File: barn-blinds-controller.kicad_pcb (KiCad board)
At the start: 4 copper layers, 65 x 73.9 mm, 112 parts, among them J1 DC005-T20, J2 USB_B_Micro, J3 Conn_01x07, J4 Phoenix Contact 1786918, Q1 2N7002, Q2 2N7002, Q3 S8050, Q4 S8050, SW1 RESET, SW2 BOOT, U1 DCDC Converter, U10 TMP235, U11 ACS723xLCTR-05AB, U12 PRTR5V0U2X, U13 PRTR5V0U2X, U14 PRTR5V0U2X, U15 PRTR5V0U2X, U2 AP2112K-3.3, U3 ESP32-S3-WROOM-1, U4 ISO7760DBQ, U5 ISO7760DBQ, U6 ISO7760DBQ, U7 AMS1117-3.3, U8 TB6612FNG, U9 TB6612FNG

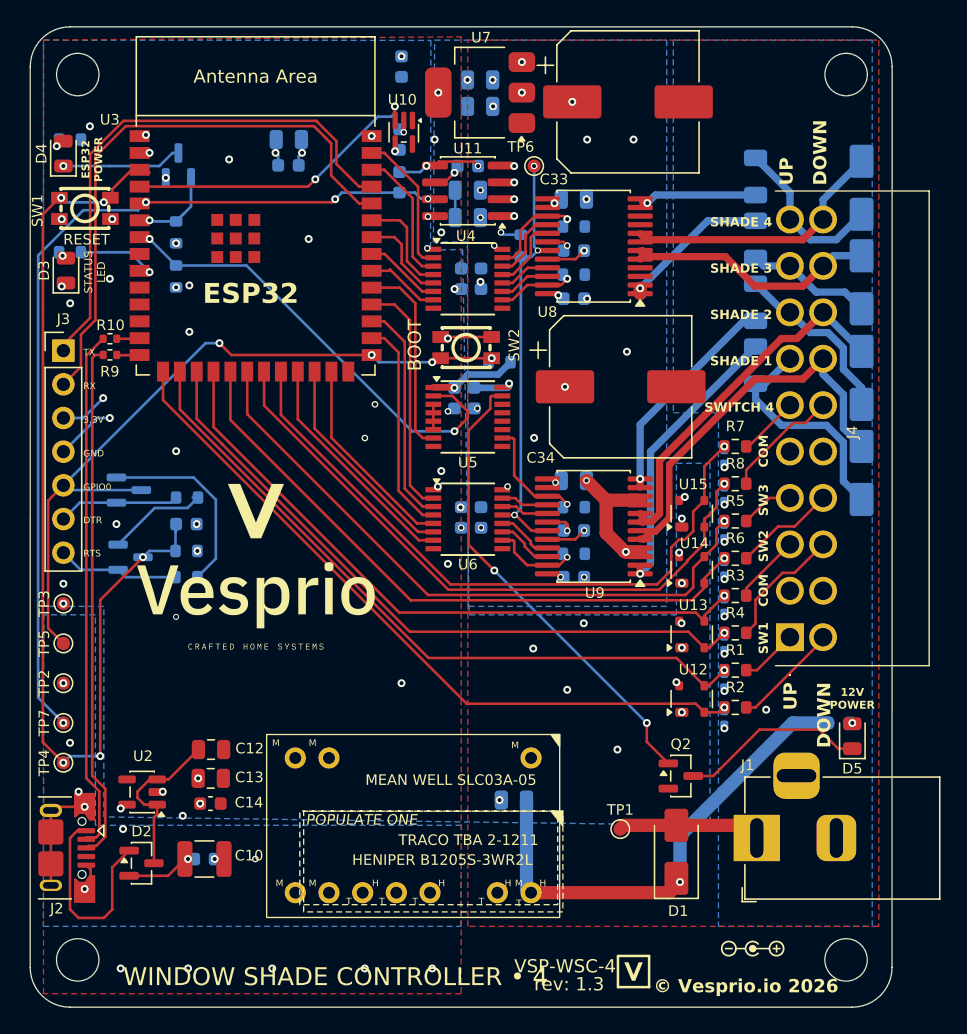
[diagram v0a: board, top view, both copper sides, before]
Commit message: Rev 1.3 PCB sync + second QA pass: BOM fixes, TVS decoupling, ERC cleanup
PCB (done in KiCad, verified here):
- F8 sync applied: D2 removed; D10/D11 (SS34 SMA) and U16 (PRTR5V0U2X SOT-143)
  placed and routed; R1-R8 -> 1k, D1 -> SS54, C10 -> 25V, U11 -> ACS725 updated
  in place. Footprint-level diff confirms exactly the intended delta, nothing
  else moved. DRC 0 errors / 0 unconnected pads.

Schematic fixes from the second QA pass:
- R1-R8 had NO LCSC part number (value change had landed, part number never
  did) - they would have come back unpopulated, silently killing the switch
  inputs. Set to C14676, matching R14's existing 1K 0603 so it consolidates to
  one BOM line. NOTE: todo.md originally specified C21190 - see the discrepancy
  note there and confirm before ordering.
- TP1-TP7 set in_bom no / in_pos_files no (were 7 junk lines in the JLCPCB BOM).
- Removed 4 orphan dangling wire stubs in switch_inputs.kicad_sch.
- Converted the orphan STBY hierarchical label in motor_drivers.kicad_sch to a
  global label rather than deleting it: its wire actually carried U9 pin 19, so
  deleting dropped U9.19 off the STBY net. Converting keeps the connection and
  clears the ERC hier_label_mismatch.
- Added C40-C43 (100nF 0402, C1525) for U12-U15 VCC decoupling. The switch-input
  TVS devices currently have their nearest +3.3V_ISO bypass 18-23mm away; a
  PRTR5V0U2X shunts ESD into VCC and needs somewhere local to dump it. Still
  need PCB placement - put each within ~2mm of its device's pin 4.

Every schematic edit was validated by diffing the exported netlist before and
after; connectivity is unchanged apart from the four intended new caps.
ERC errors: 10 -> 5 (remaining are 4x missing PWR_FLAG and one J2-GND/U1-(-Vout)
both-power-output pair that is correct by design).

Added barn-blinds-controller.kicad_dru: isolation-barrier audit rule. The board
has no dedicated ISO/MOTOR gap - minimum copper spacing between domains is
0.20mm, the global default. Rev 1.2 measured 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
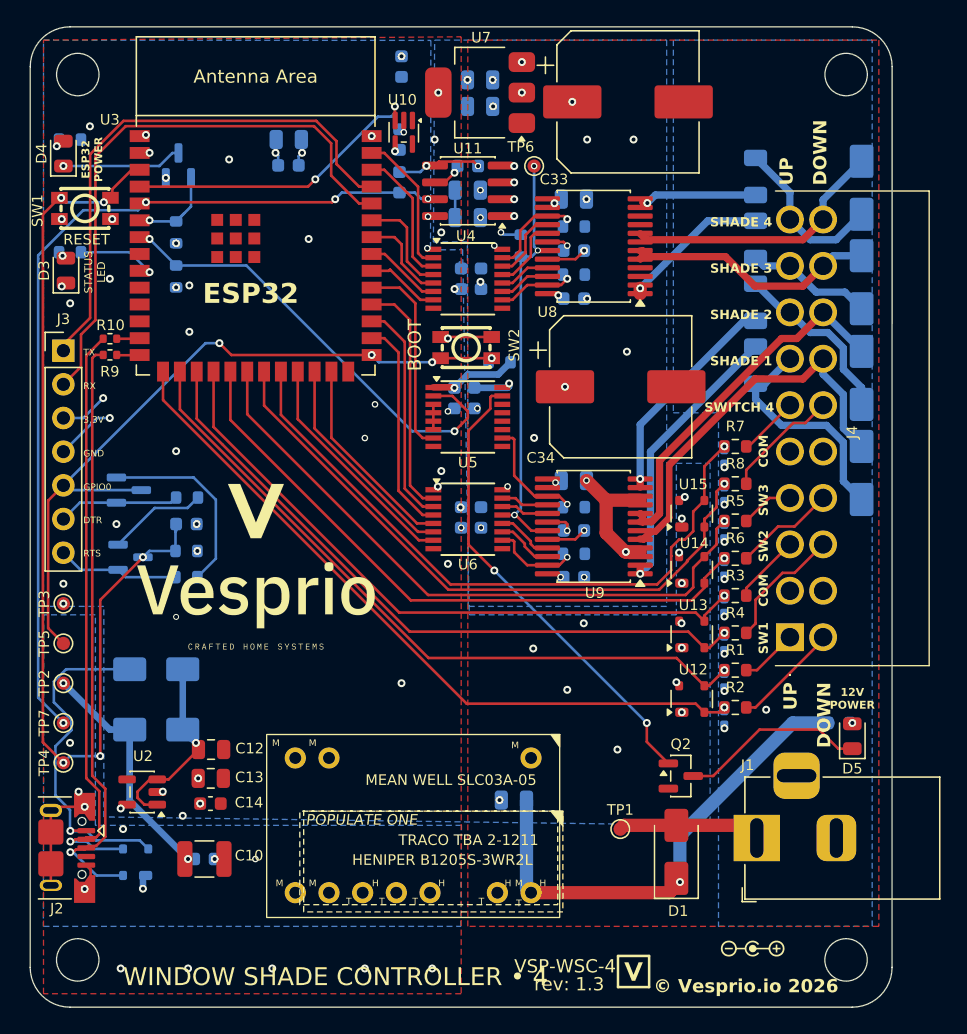
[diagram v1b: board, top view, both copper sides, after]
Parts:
- removed D2: BAT54C, Package_TO_SOT_SMD:SOT-23
- added D10: SS34, Diode_SMD:D_SMA, B.Cu at (86.5, 97.5)
- added D11: SS34, Diode_SMD:D_SMA, B.Cu at (86.5, 102.0)
- added U16: PRTR5V0U2X, Package_TO_SOT_SMD:SOT-143, B.Cu at (85.0, 112.0)
- C10: value 100uF 10V -> 100uF 25V
- D1: value SS34 -> SS54
- R1, R2, R3, R4, R5, R6, R7, R8: value 10k -> 1k
- U11: value ACS723xLCTR-05AB -> ACS725LLCTR-05AB-T
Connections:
- J2 pad 1: Net-(J2-VBUS) -> /USB-C and 5V Diode-OR/USB_VBUS
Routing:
- net /USB-C and 5V Diode-OR/USB_VBUS: track 0.00 -> 26.3 mm, vias 0 -> 1
- net Net-(J2-VBUS): track 15.5 -> 0.00 mm
- net +5V_ISO: track 4.73 -> 18.0 mm
- net USB_IN_DP: track 39.2 -> 45.1 mm, vias 0 -> 1
- net USB_IN_DN: track 39.5 -> 44.8 mm, vias 0 -> 1
- net +5V_OR: track 12.6 -> 14.0 mm, vias 0 -> 1
- net GND_ISO: track 28.5 -> 29.5 mm, vias 60 -> 61
- net DTR: track 10.1 -> 9.17 mm
- net LED_D5_CTRL: track 34.8 -> 34.2 mm
- net EN: track 74.4 -> 73.9 mm
- net BOOT: track 56.0 -> 55.5 mm

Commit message: Rev 1.3 fab-ready: PICK UP HERE items closed, JLCPCB production files generated
PCB (verified via DRC/ERC/netlist diff, not just eyeballed):
- Placed C40-C43 within ~1.8-2.6mm of each PRTR5V0U2X VCC pin (U12-U15).
- Widened +5V_OR to 0.5mm and USB_VBUS to 0.4mm.
- Moved U16 closer to J2 (center-to-center 6.1mm -> 4.0mm). Still on B.Cu
  vs J2's F.Cu, so the D+/D- path still crosses layers via a short stub -
  accepted trade-off for a Full-Speed, occasional-use flashing port.
- Fixed D10/D11 silkscreen reference overlap.
- Added LCSC to J2 (C397452, Micro-USB) and J4 (C6652293 - pre-purchased
  JLCPCB inventory part; number is still required for JLCPCB to place it).

DRC: 0 unconnected pads, 0 real errors. Remaining flagged items are all
accepted: 21 isolation-barrier warnings (all >=0.20mm, same floor as Rev 1.2)
and 5 hole_clearance exclusions on J2's own NPTH-vs-pad geometry (footprint-
inherent, not routing-fixable - confirmed the new one is capped by the same
0.20mm pad edge as the pre-existing accepted ones, not by trace width).

ERC steady at 5 benign errors (4x missing PWR_FLAG, 1x J2-GND/U1-(-Vout)
both-power-output by design).

Docs:
- Fixed stale "U7 DCDC DNP" note in jlcpcb-export-steps.md - that referred
  to a pre-renumbering designator. Today U1 is the Heniper DC-DC and U7 is
  a real, actively-used AMS1117-3.3 feeding +3.3V_MOTOR (U4-U6, U8-U9 logic
  supply) that must NOT be DNP'd.
- Documented U1's actual situation instead: DCDC_HYBRID_SLC03_TEC2 is a
  shared THT footprint across three vendor DC-DC modules (Mean Well/Traco/
  Heniper), silkscreened per-hole M/H/T. This run uses the Heniper
  (C20622657, JLCPCB inventory). Same-numbered pads share nets regardless
  of vendor so there's no electrical risk, but BOM/CPL only carry one
  position+rotation for the whole footprint - added a note that the JLCPCB
  assembly order needs an explicit remark to populate only the H holes.
- Updated CLAUDE.md PICK UP HERE and vsp-wsc4-todo.md to reflect fab-ready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
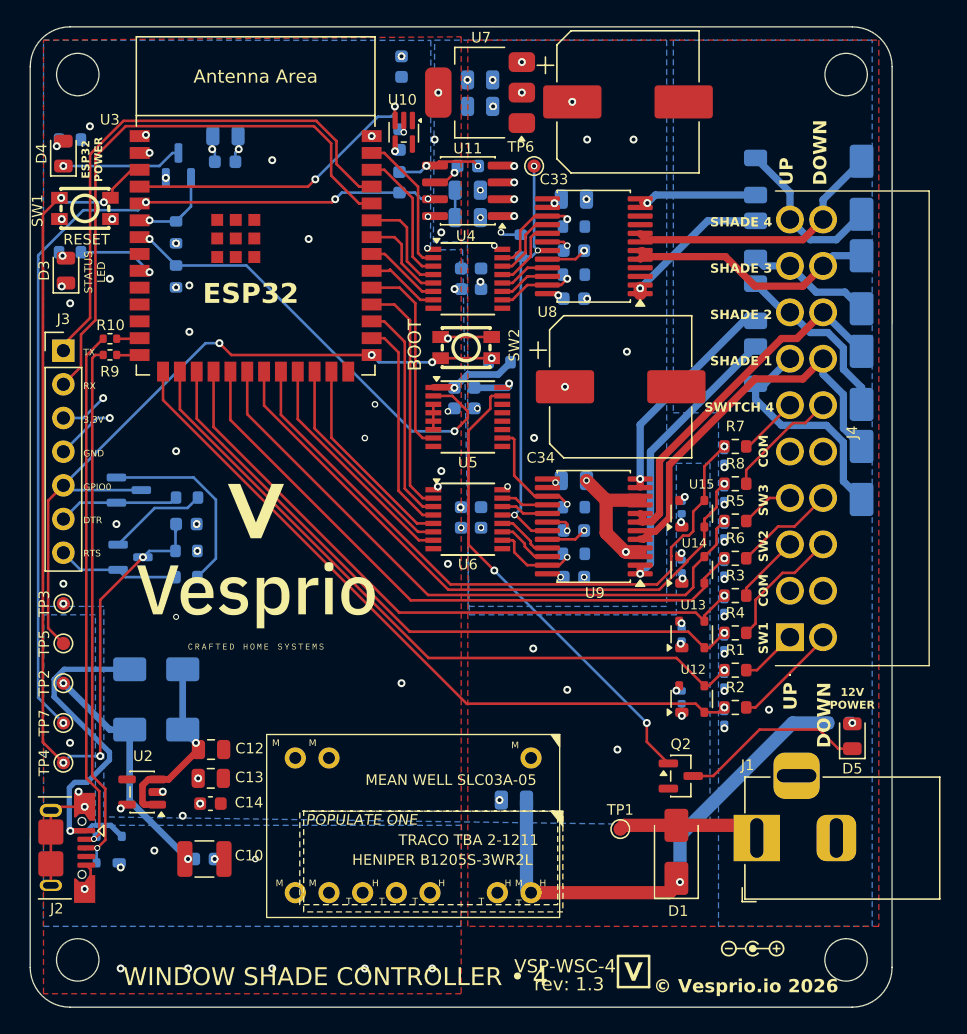
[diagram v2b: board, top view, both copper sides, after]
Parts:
- added C40: 100nF, Capacitor_SMD:C_0402_1005Metric, B.Cu at (126.1, 99.6)
- added C41: 100nF, Capacitor_SMD:C_0402_1005Metric, B.Cu at (126.1, 94.8)
- added C42: 100nF, Capacitor_SMD:C_0402_1005Metric, B.Cu at (126.1, 89.7)
- added C43: 100nF, Capacitor_SMD:C_0402_1005Metric, B.Cu at (126.1, 85.2)
- moved C15 4.78 mm to (91.7, 59.2)
- moved C16 4.78 mm to (91.7, 57.2)
- moved U16 2.21 mm to (83.0, 111.1)
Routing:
- net USB_IN_DN: track 44.8 -> 38.8 mm
- net USB_IN_DP: track 45.1 -> 39.8 mm
- net GND_ISO: track 29.5 -> 30.0 mm
- net +3.3V_ISO: track 12.7 -> 13.3 mm
- net GND_MOTOR: vias 24 -> 23

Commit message: Stock-driven part swaps (C10, U12-U16) + J3 DNP after BOM audit
C10 (isolated 5V_ISO bulk cap): 100uF 25V (C2840614) was out of stock at
JLCPCB. Swapped to 100uF 16V (C7432790, HGC1210R5107M160NSVK) - same 1210
footprint, no PCB rework. 16V chosen over 10V/6.3V alternatives to keep
DC-bias derating low on the ~5V rail (unregulated B1205S-3WR2L output).

U12-U16 (PRTR5V0U2X ESD protection): C12333 was out of stock. Swapped to
C5158049 (UMW/Youtai) - same SOT-143 footprint, no PCB rework. Checked
four other "PRTR5V0U2X"-labeled LCSC listings before picking this one -
they were mismatched (unidirectional, or 14-25V standoff instead of ~5V)
despite sharing the part name; C5158049 actually matches the real
bidirectional/0.35pF/5V-7.2V spec.

Both changes verified via netlist diff (only Value/LCSC fields changed,
zero connectivity impact) and ERC (still 5 known-benign errors).

Auditing the regenerated JLCPCB assembly-order BOM turned up a separate,
pre-existing bug: J3's LCSC (C492404) is a 5-pin header (PZ254V-11-05P),
mismatched against its 7-pin footprint - a leftover from before J3 grew
from 5->7 pins for the RTS/DTR rework, where the LCSC field (and a stale
"01x05" Description) never got updated. JLCPCB's assembly matcher didn't
flag the mismatch, it silently auto-substituted a different 5-pin part.
A real 7-pin replacement isn't in stock either, and J3 is only a backup
UART flashing path (native USB on GPIO19/20 is primary) - not worth
chasing for this run, so J3 is now marked DNP. Fixed the stale "01x05"
Description text to "01x07" so the record is correct if it's ever
un-DNP'd (LCSC still needs a real 7-pin part first if that happens).

PCB: C10/U12-U16 changes synced via F8. J3's new DNP flag still needs an
F8 sync (done after the schematic edit, not yet reflected on the board).

Updated CLAUDE.md PICK UP HERE and vsp-wsc4-todo.md with full detail.
VSP-WSC-4_1.3 production files predate all three changes - needs a
Fabrication Toolkit re-run before ordering.

Co-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
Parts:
- C10: value 100uF 25V -> 100uF 16V
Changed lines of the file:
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@@
 			)
 		)
-		(property "Value" "100uF 25V"
+		(property "Value" "100uF 16V"
 			(at 0 2.3 0)
 			(layer "F.Fab")
@@
 			)
 		)
-		(property "LCSC" "C2840614"
+		(property "LCSC" "C7432790"
 			(at 0 0 0)
 			(unlocked yes)
@@
 			)
 		)
-		(property "LCSC" "C12333"
+		(property "LCSC" "C5158049"
 			(at 0 0 90)
 			(unlocked yes)
@@
 			)
 		)
-		(property "LCSC" "C12333"
+		(property "LCSC" "C5158049"
 			(at 0 0 90)
 			(unlocked yes)
@@
 			)
 		)
-		(property "LCSC" "C12333"
+		(property "LCSC" "C5158049"
 			(at 0 0 90)
 			(unlocked yes)
@@
 			)
 		)
-		(property "LCSC" "C12333"
+		(property "LCSC" "C5158049"
 			(at 0 0 90)
 			(unlocked yes)
@@
 			)
 		)
-		(property "LCSC" "C12333"
+		(property "LCSC" "C5158049"
 			(at 0 0 270)
 			(unlocked yes)
